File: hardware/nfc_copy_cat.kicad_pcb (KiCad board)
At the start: 2 copper layers, 40.4 x 43 mm, 41 parts, among them J1 USB_B_Micro, J2 Battery, J3 SWD, J4 NFC Module V3, J5 Conn_01x02, J6 Adafruit NFC 1.0, SW1 RST, SW2 Magspoof, SW3 NFC, U1 AP2112K-3.3TRG1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

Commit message: fix usb and leds
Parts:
- D1, D3, D4, D5, D6, SW1, SW2, SW3: moved to B.Cu
- moved C3 59.1 mm to (153.2, 55.3), turned to 180 degrees
- moved R7 58.7 mm to (153.1, 59.1), turned to 180 degrees
- moved U5 50.5 mm to (150.6, 65.0)
- moved J2 33.5 mm to (136.3, 90.1), turned to 270 degrees
- moved C4 32.4 mm to (145.7, 54.5), turned to 0 degrees
- moved C1 30.3 mm to (145.7, 56.7), turned to 0 degrees
- moved J1 23.3 mm to (144.4, 88.2), turned to 0 degrees
- moved G*** 23.0 mm to (140.5, 38.9)
- moved C7 18.0 mm to (133.7, 75.6), turned to 180 degrees
- moved R6 17.3 mm to (138.6, 51.7)
- moved D2 17.2 mm to (129.2, 68.9), turned to 270 degrees
- moved D6 17.1 mm to (138.6, 51.7)
- moved U2 14.9 mm to (133.9, 71.9), turned to 90 degrees
- moved R3 13.9 mm to (138.1, 75.6), turned to 180 degrees
- moved R4 12.1 mm to (138.6, 57.3), turned to 180 degrees
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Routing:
- net GND: track 0.91 -> 9.74 mm, vias 1 -> 0
- net Net-(D1-Pad1): track 0.01 -> 3.03 mm, vias 0 -> 1
- net Net-(D4-Pad1): track 0.00 -> 2.79 mm, vias 0 -> 1
- net Net-(D6-Pad1): track 0.01 -> 2.72 mm, vias 0 -> 1
- net Net-(D5-Pad1): track 0.00 -> 2.17 mm, vias 0 -> 1

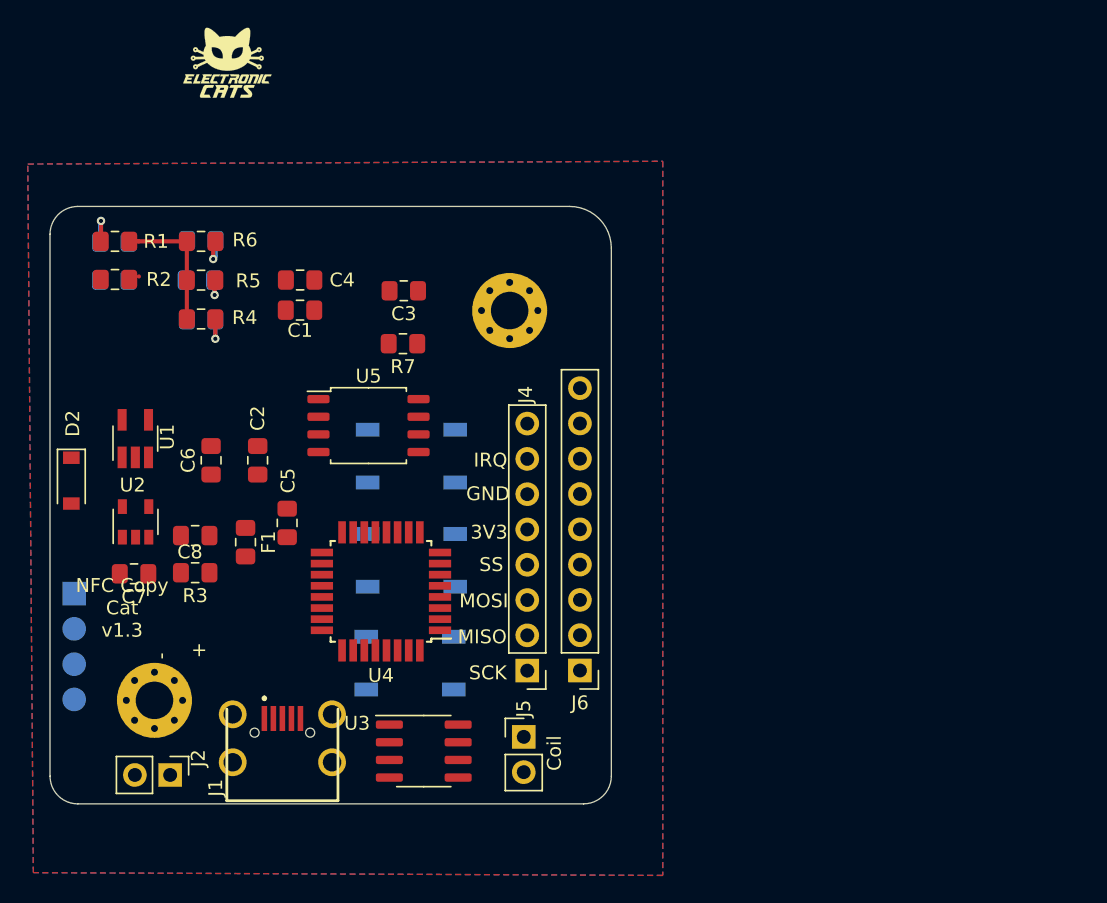
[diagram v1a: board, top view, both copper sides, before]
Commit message: routeo charger
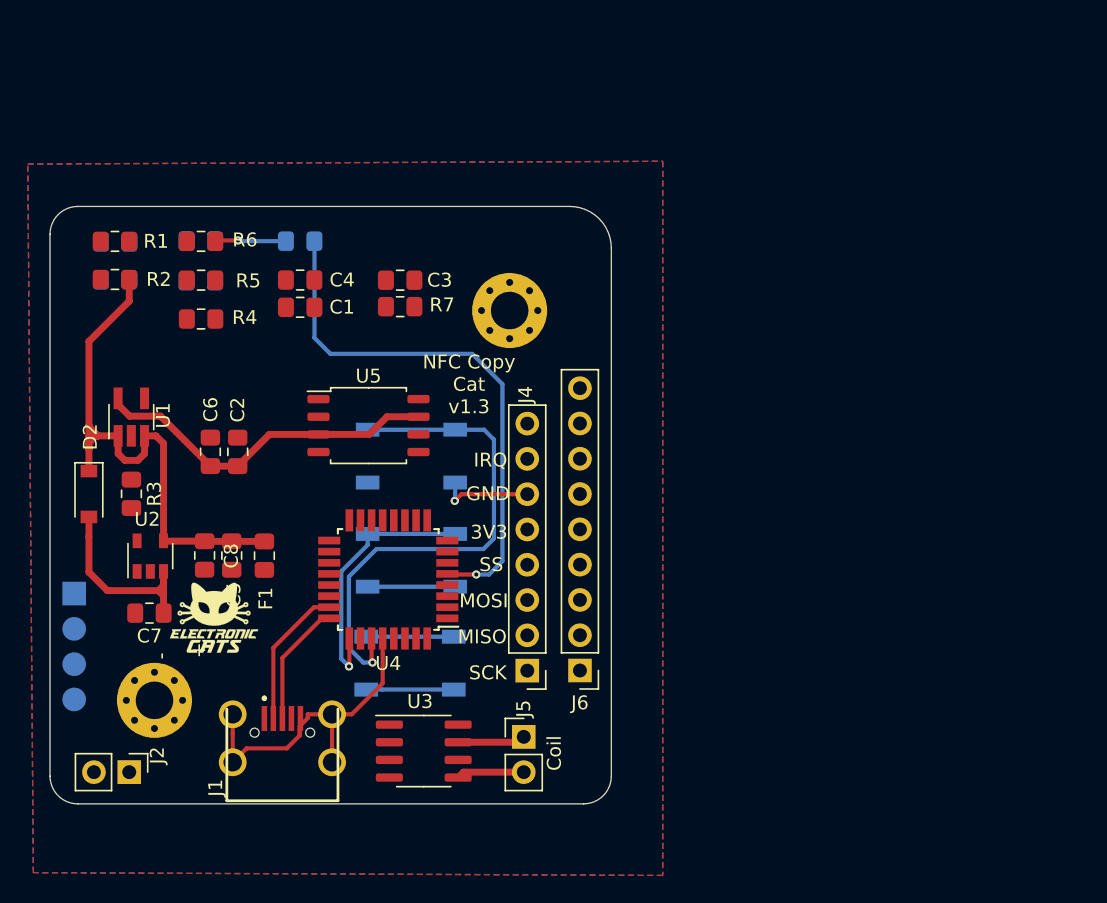
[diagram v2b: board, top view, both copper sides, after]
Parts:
- moved G*** 40.0 mm to (139.5, 78.8)
- moved REF** 16.3 mm to (142.9, 64.6)
- moved R3 7.30 mm to (133.6, 69.9), turned to 270 degrees
- moved D6 7.11 mm to (145.7, 51.7), turned to 0 degrees
- moved C5 4.63 mm to (140.8, 74.3)
- moved C7 3.04 mm to (134.9, 78.5)
- moved G*** 3.00 mm to (143.8, 72.6)
- moved J2 2.95 mm to (133.4, 89.9)
- moved D5 2.82 mm to (138.5, 51.7)
- moved D4 2.81 mm to (138.5, 54.5)
- moved U2 2.68 mm to (134.9, 74.4)
- moved R7 2.67 mm to (152.9, 56.4)
- moved F1 1.67 mm to (143.1, 74.3)
- moved D2 1.59 mm to (130.5, 69.9)
- moved C8 1.58 mm to (138.8, 74.3), turned to 270 degrees
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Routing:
- net VCC: track 0.01 -> 40.7 mm
- net /LED3: track 0.00 -> 39.0 mm, vias 0 -> 1
- net /SW2: track 0.00 -> 37.1 mm, vias 0 -> 1
- net GND: track 9.74 -> 43.7 mm, vias 0 -> 1
- net +3V3: track 0.00 -> 25.4 mm
- net /SW1: track 0.00 -> 18.9 mm, vias 0 -> 1
- net +BATT: track 0.00 -> 14.5 mm
- net /D-: track 0.00 -> 10.3 mm
- net /D+: track 0.00 -> 8.91 mm
- net /RESET: track 0.00 -> 6.30 mm
- net /OUTB: track 0.00 -> 4.88 mm
- net /OUTA: track 0.00 -> 4.88 mm
- net Net-(D1-Pad1): track 3.03 -> 0.00 mm, vias 1 -> 0
- net Net-(D4-Pad1): track 2.79 -> 0.00 mm, vias 1 -> 0
- net Net-(D6-Pad1): track 2.72 -> 5.13 mm
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
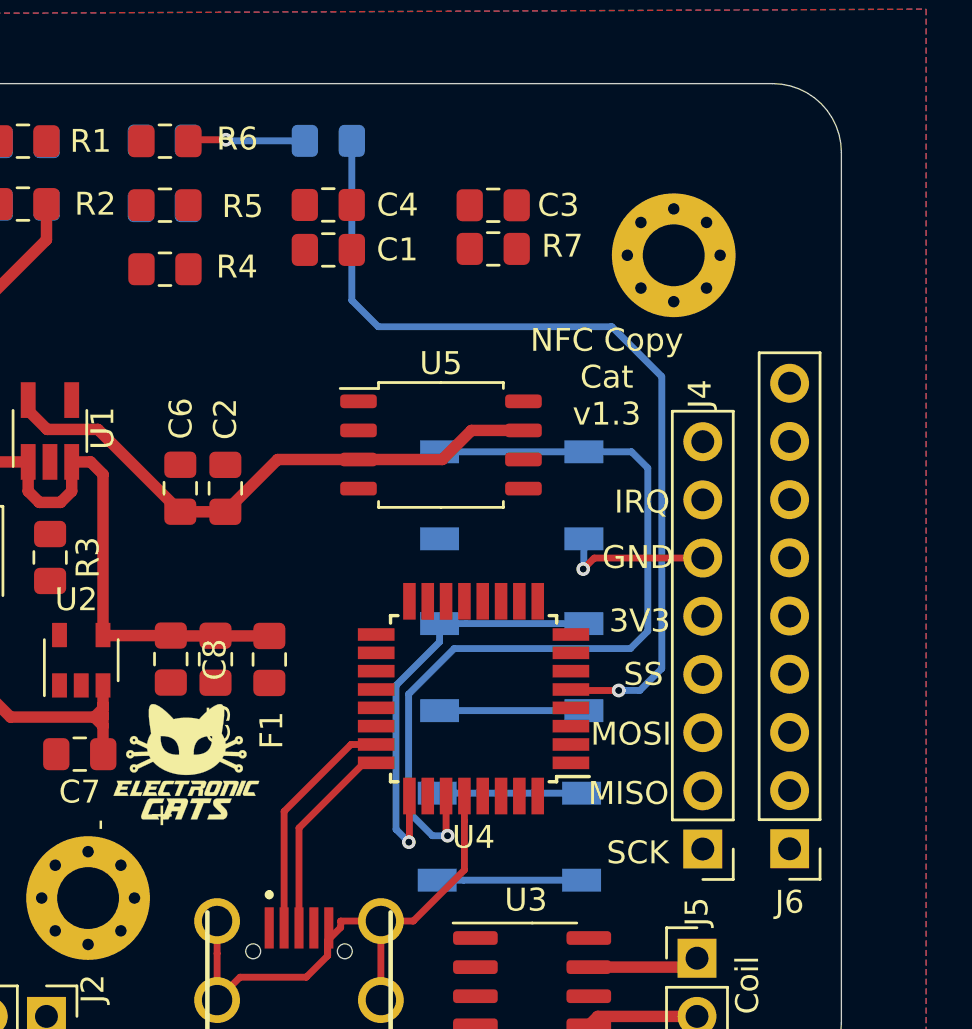
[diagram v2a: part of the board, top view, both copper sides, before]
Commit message: fix push and routeo samd
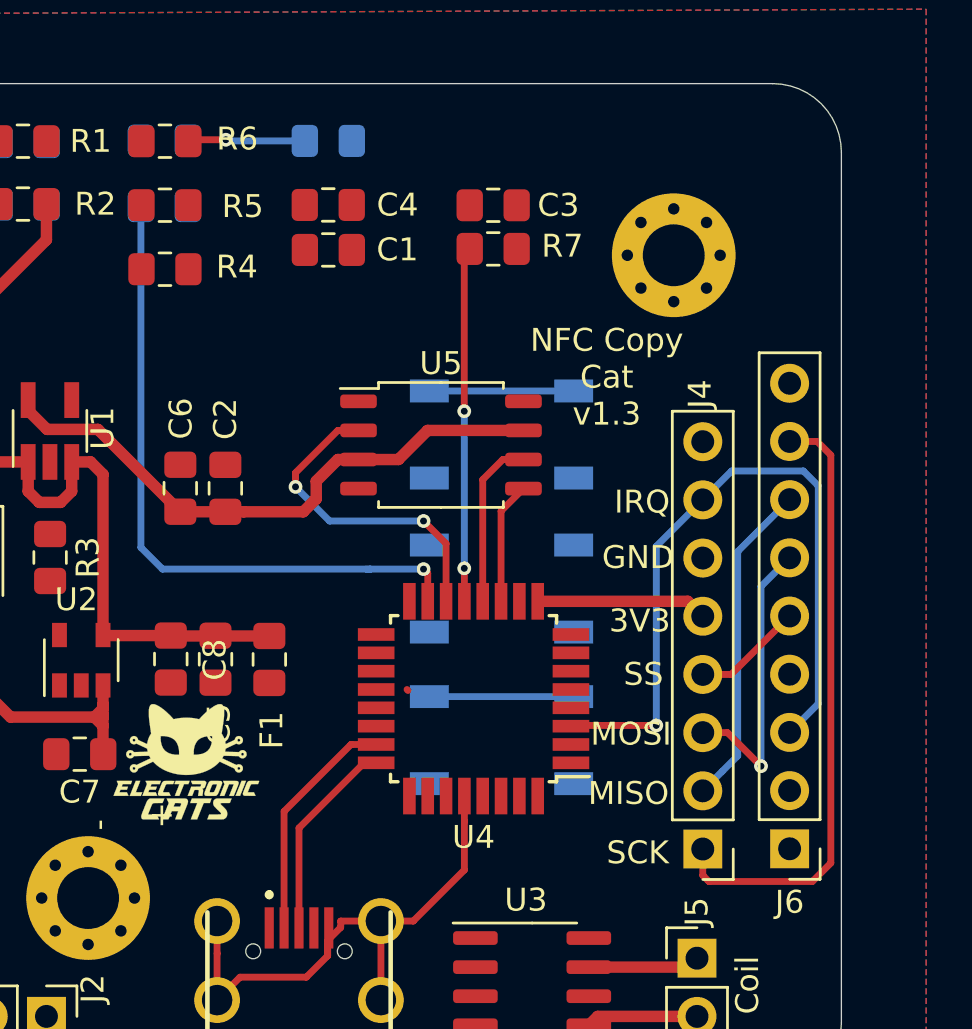
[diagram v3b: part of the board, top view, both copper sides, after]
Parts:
- moved SW1 4.23 mm to (153.3, 77.9)
- moved SW2 3.46 mm to (153.3, 71.2)
- moved SW3 2.69 mm to (153.3, 64.5)
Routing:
- net /LED3: track 39.0 -> 0.06 mm, vias 1 -> 0
- net /IRQ: track 0.00 -> 31.5 mm, vias 0 -> 1
- net /SW2: track 37.1 -> 6.30 mm, vias 1 -> 0
- net /LED1: track 0.00 -> 29.3 mm, vias 0 -> 1
- net /13(SCK): track 0.00 -> 27.0 mm
- net GND: track 43.7 -> 24.3 mm, vias 1 -> 0
- net /SW1: track 18.9 -> 0.00 mm, vias 1 -> 0
- net /SS: track 0.00 -> 15.5 mm, vias 0 -> 2
- net /12(MISO): track 0.00 -> 14.3 mm
- net /MISO: track 0.00 -> 14.2 mm, vias 0 -> 2
- net /11(MOSI): track 0.00 -> 12.8 mm, vias 0 -> 1
- net +3V3: track 25.4 -> 33.3 mm
- net /SCK: track 0.00 -> 7.45 mm
- net /MOSI: track 0.00 -> 5.32 mm
- net /10(SS): track 0.00 -> 4.85 mm

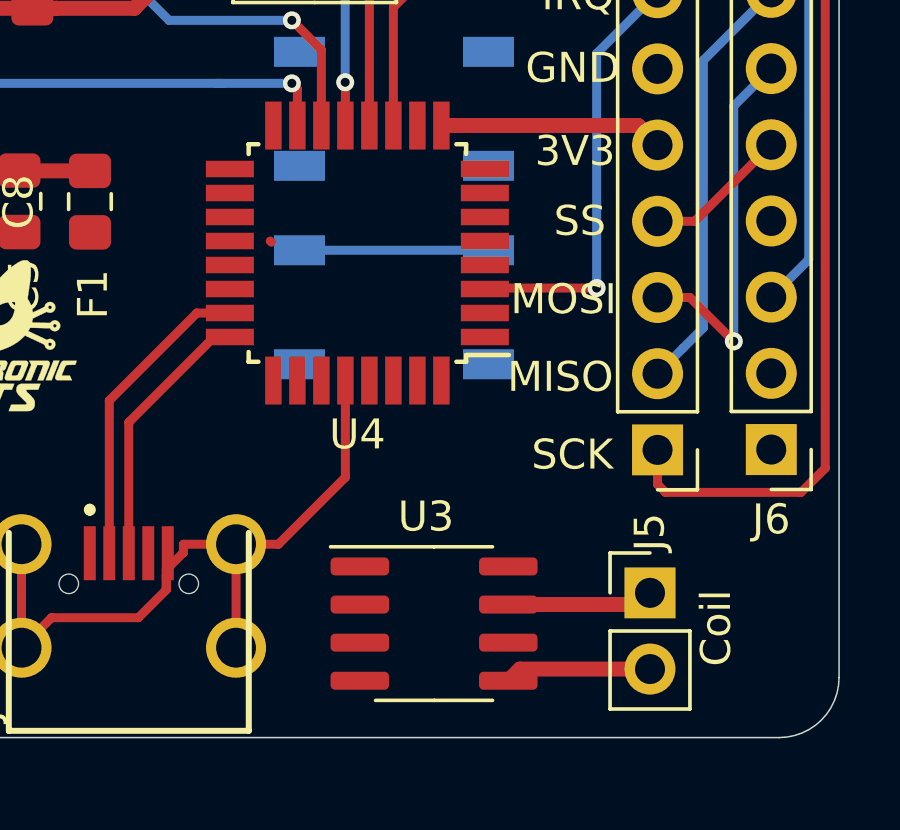
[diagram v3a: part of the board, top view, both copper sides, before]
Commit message: TC4424
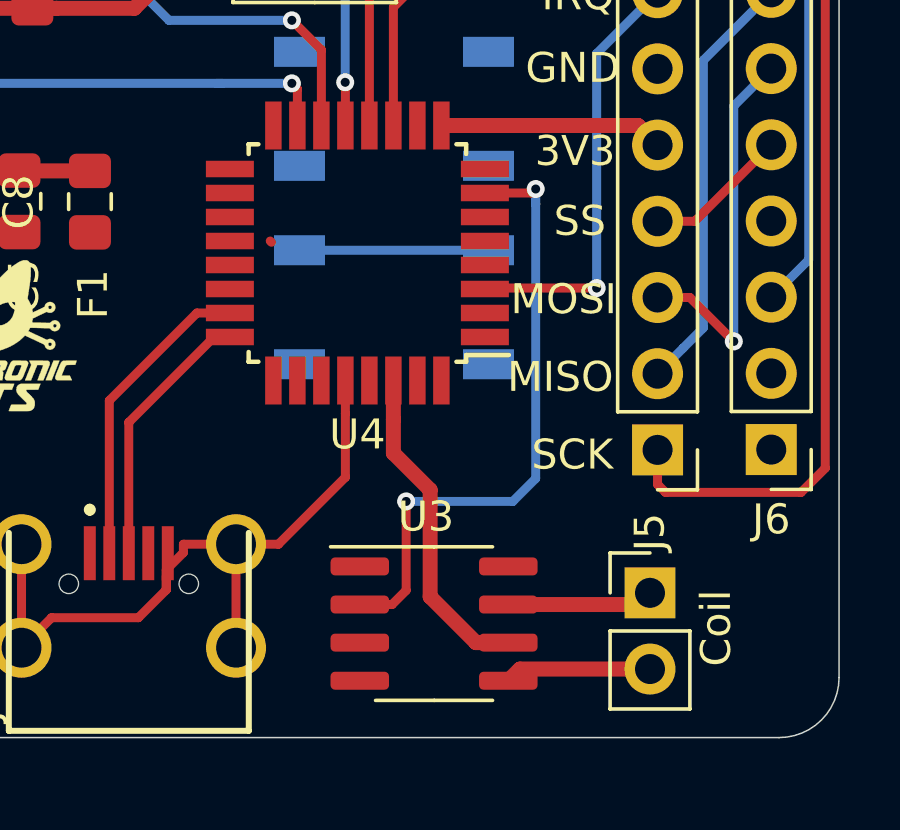
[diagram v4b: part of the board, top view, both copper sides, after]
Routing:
- net /IN_A: track 0.00 -> 21.0 mm, vias 0 -> 2
- net +3V3: track 33.3 -> 44.3 mm
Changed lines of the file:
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@@
     (thickness 1.6)
     (drawings 28)
-    (tracks 155)
+    (tracks 173)
     (zones 0)
     (modules 41)
@@
     (tags "LED handsolder")
     (attr smd)
-    (fp_text reference D6 (at -3.0898 0) (layer B.SilkS)
+    (fp_text reference D6 (at 3.139 -0.138) (layer B.SilkS)
       (effects (font (size 1 1) (thickness 0.15)) (justify mirror))
     )
@@
   (segment (start 161.3976 71.7976) (end 162.05 72.45) (width 0.5) (layer F.Cu) (net 1))
   (segment (start 154.8444 71.7976) (end 161.3976 71.7976) (width 0.5) (layer F.Cu) (net 1))
+  (segment (start 156 89.035) (end 154.470002 87.505002) (width 0.5) (layer F.Cu) (net 1))
+  (segment (start 153.2444 82.718396) (end 153.2444 81.5976) (width 0.5) (layer F.Cu) (net 1))
+  (segment (start 154.470002 87.505002) (end 154.470002 83.943998) (width 0.5) (layer F.Cu) (net 1))
+  (segment (start 157.075 89.035) (end 156 89.035) (width 0.5) (layer F.Cu) (net 1))
+  (segment (start 154.470002 83.943998) (end 153.2444 82.718396) (width 0.5) (layer F.Cu) (net 1))
+  (segment (start 153.2444 81.5976) (end 153.2444 80.2976) (width 0.5) (layer F.Cu) (net 1))
   (segment (start 147.9994 89.2046) (end 147.9994 85.7546) (width 0.3) (layer F.Cu) (net 2))
   (segment (start 140.8494 87.168813) (end 140.8494 89.2046) (width 0.3) (layer F.Cu) (net 2))
@@
   (segment (start 161.798 89.916) (end 157.464 89.916) (width 0.5) (layer F.Cu) (net 19))
   (segment (start 150.114 75.956) (end 156.414 75.956) (width 0.3) (layer B.Cu) (net 21))
+  (segment (start 153.67 87.295) (end 153.67 84.328) (width 0.3) (layer F.Cu) (net 23))
+  (segment (start 153.2 87.765) (end 153.67 87.295) (width 0.3) (layer F.Cu) (net 23))
+  (segment (start 152.125 87.765) (end 153.2 87.765) (width 0.3) (layer F.Cu) (net 23))
+  (via (at 153.67 84.328) (size 0.6) (drill 0.3) (layers F.Cu B.Cu) (net 23))
+  (segment (start 153.67 84.328) (end 157.226 84.328) (width 0.3) (layer B.Cu) (net 23))
+  (via (at 157.988 73.914) (size 0.6) (drill 0.3) (layers F.Cu B.Cu) (net 23))
+  (segment (start 157.226 84.328) (end 157.988 83.566) (width 0.3) (layer B.Cu) (net 23))
+  (segment (start 157.988 74.422) (end 157.988 73.914) (width 0.3) (layer B.Cu) (net 23))
+  (segment (start 157.988 83.566) (end 157.988 74.422) (width 0.3) (layer B.Cu) (net 23))
+  (segment (start 157.988 74.422) (end 157.988 74.168) (width 0.3) (layer B.Cu) (net 23))
+  (segment (start 157.8544 74.0476) (end 157.988 73.914) (width 0.3) (layer F.Cu) (net 23))
+  (segment (start 156.2944 74.0476) (end 157.8544 74.0476) (width 0.3) (layer F.Cu) (net 23))
   (segment (start 150.114 62.616) (end 156.414 62.616) (width 0.3) (layer B.Cu) (net 33))
   (segment (start 135.87 78.46) (end 135.88 78.47) (width 0.5) (layer F.Cu) (net 37))

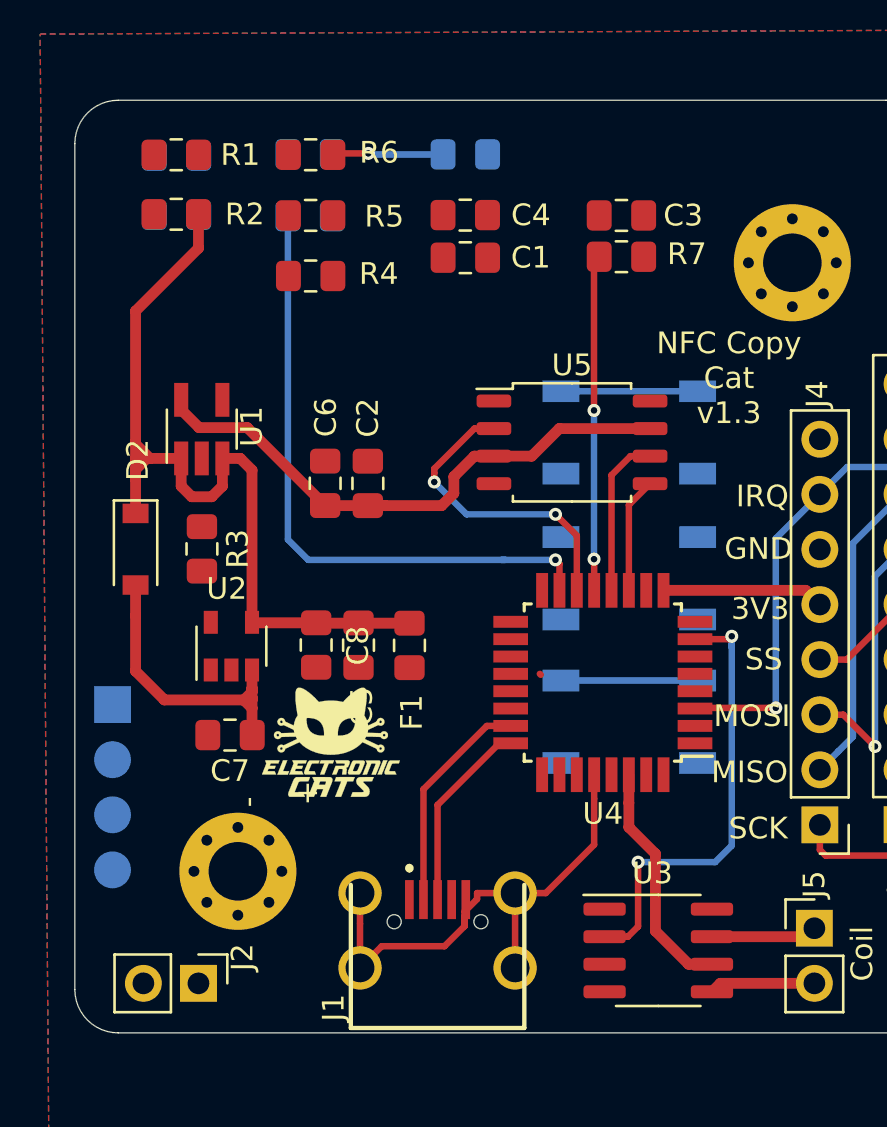
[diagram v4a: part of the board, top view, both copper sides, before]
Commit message: change leds and res
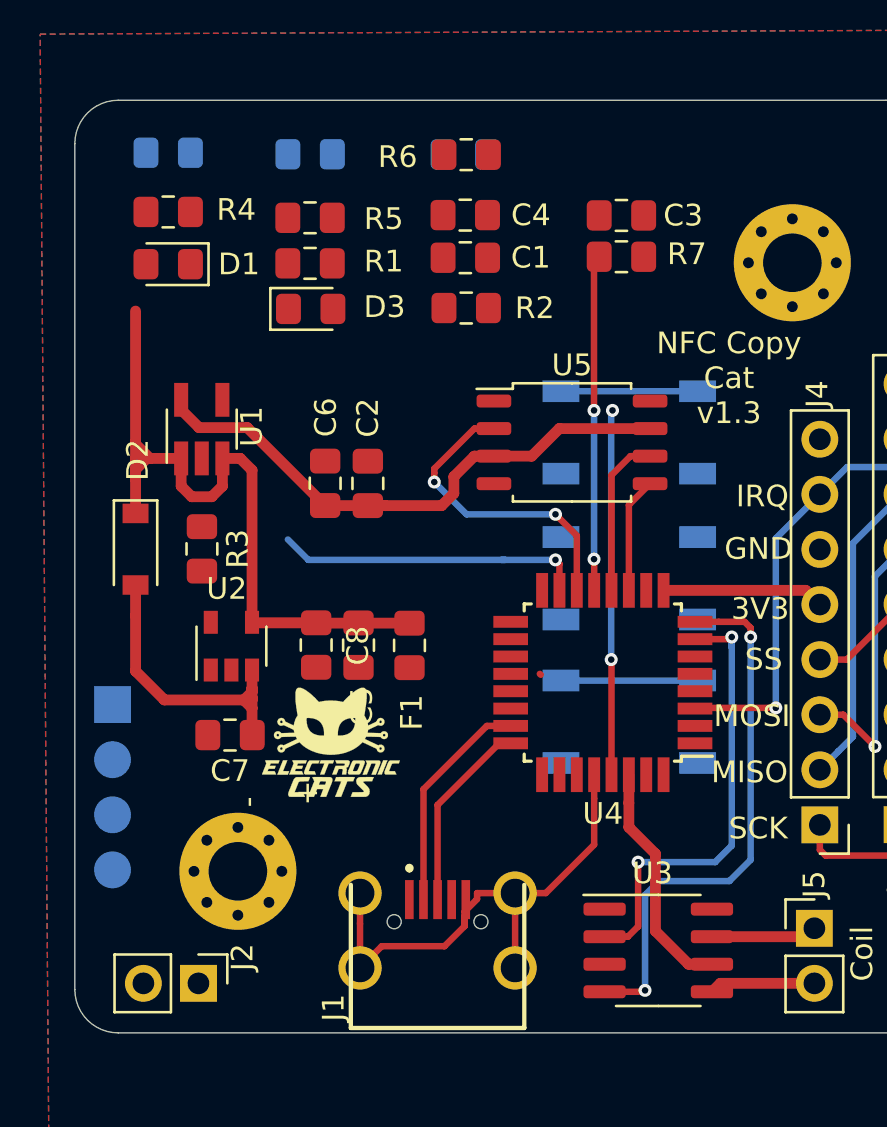
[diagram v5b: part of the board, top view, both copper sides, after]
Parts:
- D1, D3: moved to F.Cu
- moved R2 14.1 mm to (145.7, 58.8)
- moved R1 7.94 mm to (138.5, 56.7)
- moved D3 7.56 mm to (138.6, 58.8)
- moved R4 7.20 mm to (132.0, 54.4)
- moved R6 7.17 mm to (145.7, 51.7), turned to 0 degrees
- moved D4 7.17 mm to (132.0, 51.6)
- moved D1 5.02 mm to (132.0, 56.8), turned to 180 degrees
- moved R5 0.12 mm to (138.5, 54.6)
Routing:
- net /IN_B: track 0.00 -> 25.2 mm, vias 0 -> 2
- net Net-(C1-Pad1): track 0.00 -> 16.8 mm, vias 0 -> 2
- net /LED1: track 29.3 -> 14.4 mm
- net VCC: track 40.7 -> 35.1 mm
- net Net-(D6-Pad1): track 5.13 -> 0.00 mm, vias 1 -> 0
